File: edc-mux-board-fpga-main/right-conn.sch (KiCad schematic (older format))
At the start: 75 parts, among them J10 Device 7, J6 Power In, J7 Device 4, J8 Device 5, J9 Device 6, Q3 CSD18501Q5A, SW1 Power Switch, U1 LM74610-Q1, U33 R-78B12-2.0

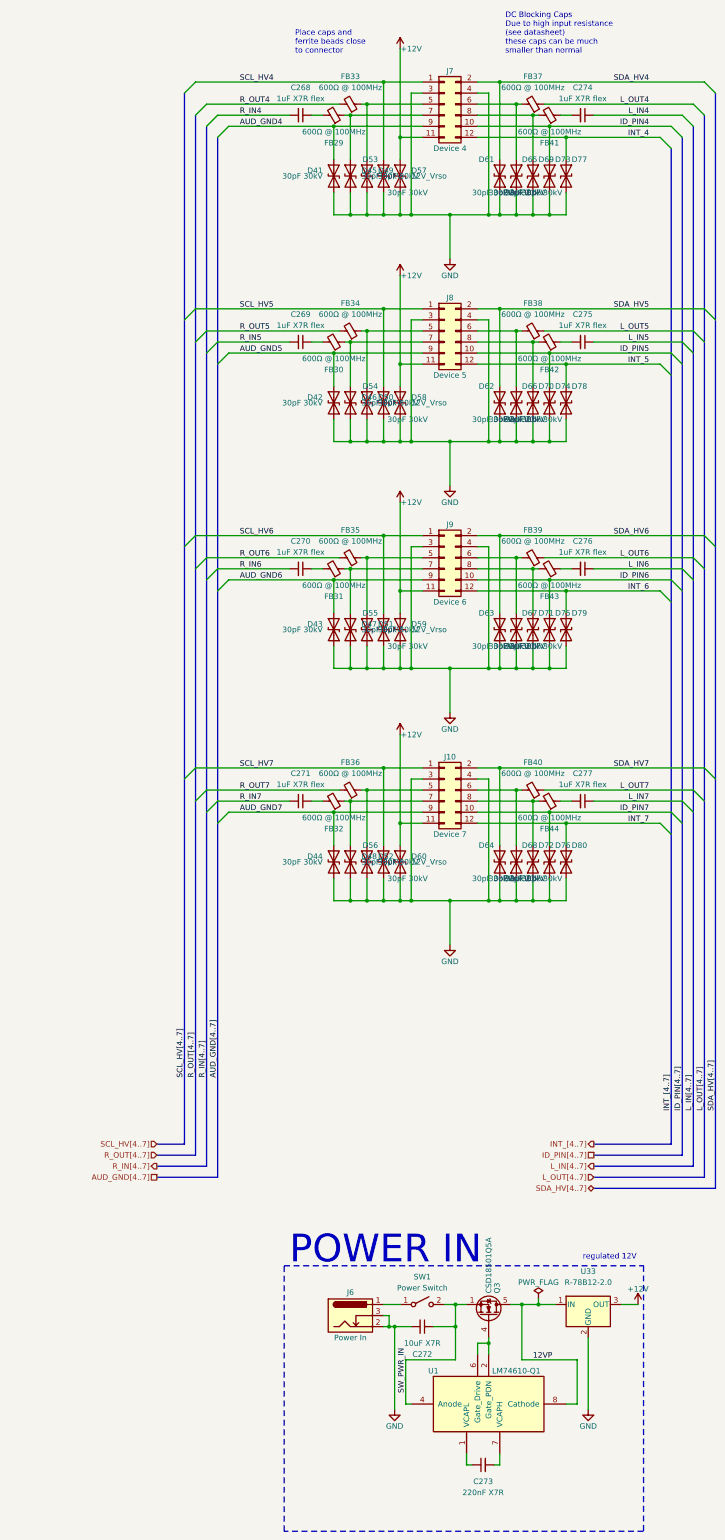
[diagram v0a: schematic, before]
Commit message: migrating right-conn changes from expansion to main
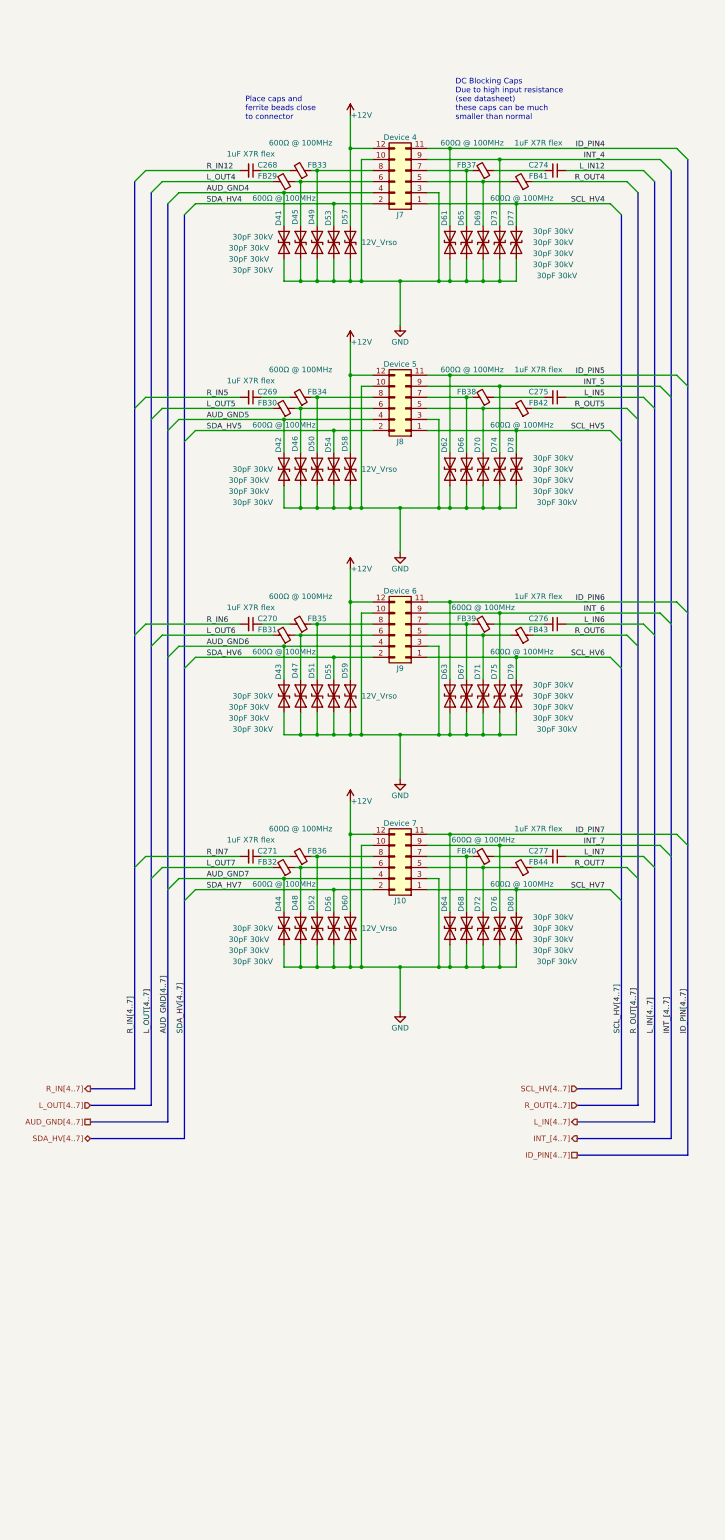
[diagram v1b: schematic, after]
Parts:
- removed C272: 10uF X7R, Capacitor_SMD:C_1206_3216Metric, symbol Device:C_Small
- removed C273: 220nF X7R, Capacitor_SMD:C_0603_1608Metric, symbol Device:C_Small
- removed J6: Power In, SW-Switchcraft:PCL712AS, symbol Connector:Barrel_Jack_Switch
- removed Q3: CSD18501Q5A, Package_TO_SOT_SMD:TDSON-8-1, symbol Transistor_FET:CSD18501Q5A
- removed SW1: Power Switch, Connector_PinHeader_2.54mm:PinHeader_1x02_P2.54mm_Vertical, symbol Switch:SW_SPST
- removed U1: LM74610-Q1, Package_SO:VSSOP-8_3.0x3.0mm_P0.65mm, symbol SW-Texas:LM74610-Q1
- removed U33: R-78B12-2.0, Converter_DCDC:Converter_DCDC_RECOM_R-78B-2.0_THT, symbol Regulator_Switching:R-78B12-2.0
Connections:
- net +12V: now also J10.12 (Pin_12), J7.12 (Pin_12), J8.12 (Pin_12), J9.12 (Pin_12); no longer J10.11 (Pin_11), J7.11 (Pin_11), J8.11 (Pin_11), J9.11 (Pin_11)
- net AUD_GND4: now also J7.4 (Pin_4); no longer J7.9 (Pin_9)
- net AUD_GND5: now also J8.4 (Pin_4); no longer J8.9 (Pin_9)
- net AUD_GND6: now also J9.4 (Pin_4); no longer J9.9 (Pin_9)
- net AUD_GND7: now also J10.4 (Pin_4); no longer J10.9 (Pin_9)
- net GND: now also J10.10 (Pin_10), J7.10 (Pin_10), J8.10 (Pin_10), J9.10 (Pin_10); no longer J10.4 (Pin_4), J7.4 (Pin_4), J8.4 (Pin_4), J9.4 (Pin_4)
- net ID_PIN4: now also D61.1 (A1), J7.11 (Pin_11); no longer D73.1 (A1), J7.10 (Pin_10)
- net ID_PIN5: now also D62.1 (A1), J8.11 (Pin_11); no longer D74.1 (A1), J8.10 (Pin_10)
- net ID_PIN6: now also D63.1 (A1), J9.11 (Pin_11); no longer D75.1 (A1), J9.10 (Pin_10)
- net ID_PIN7: now also D64.1 (A1), J10.11 (Pin_11); no longer D76.1 (A1), J10.10 (Pin_10)
- net INT_4: now also D73.1 (A1), J7.9 (Pin_9); no longer D77.1 (A1), J7.12 (Pin_12)
- net INT_5: now also D74.1 (A1), J8.9 (Pin_9); no longer D78.1 (A1), J8.12 (Pin_12)
- net INT_6: now also D75.1 (A1), J9.9 (Pin_9); no longer D79.1 (A1), J9.12 (Pin_12)
- net INT_7: now also D76.1 (A1), J10.9 (Pin_9); no longer D80.1 (A1), J10.12 (Pin_12)
- net L_OUT4: now also FB29.2; no longer FB37.1
- net L_OUT5: now also FB30.2; no longer FB38.1
- net L_OUT6: now also FB31.2; no longer FB39.1
- net L_OUT7: now also FB32.2; no longer FB40.1
- net R_OUT4: now also FB41.1; no longer FB33.2
- net R_OUT5: now also FB42.1; no longer FB34.2
- net R_OUT6: now also FB43.1; no longer FB35.2
- net R_OUT7: now also FB44.1; no longer FB36.2
- net SCL_HV4: now also D77.1 (A1); no longer D53.1 (A1)
- net SCL_HV5: now also D78.1 (A1); no longer D54.1 (A1)
- net SCL_HV6: now also D79.1 (A1); no longer D55.1 (A1)
- net SCL_HV7: now also D80.1 (A1); no longer D56.1 (A1)
- net SDA_HV4: now also D53.1 (A1); no longer D61.1 (A1)
- net SDA_HV5: now also D54.1 (A1); no longer D62.1 (A1)
- net SDA_HV6: now also D55.1 (A1); no longer D63.1 (A1)
- net SDA_HV7: now also D56.1 (A1); no longer D64.1 (A1)
- net at D49.1 (A1), FB33.1: now also J7.8 (Pin_8); no longer J7.5 (Pin_5)
- net at D65.1 (A1), FB37.2: now also J7.7 (Pin_7); no longer J7.6 (Pin_6)
- net at D45.1 (A1), FB29.1: now also J7.6 (Pin_6); no longer J7.7 (Pin_7)
- net at D69.1 (A1), FB41.2: now also J7.5 (Pin_5); no longer J7.8 (Pin_8)
- net at C268.1: now also FB33.2; no longer FB29.2
- net at C274.2: now also FB37.1; no longer FB41.1
- net at D50.1 (A1), FB34.1: now also J8.8 (Pin_8); no longer J8.5 (Pin_5)
- net at D66.1 (A1), FB38.2: now also J8.7 (Pin_7); no longer J8.6 (Pin_6)
- net at D46.1 (A1), FB30.1: now also J8.6 (Pin_6); no longer J8.7 (Pin_7)
- net at D70.1 (A1), FB42.2: now also J8.5 (Pin_5); no longer J8.8 (Pin_8)
- net at C269.1: now also FB34.2; no longer FB30.2
- net at C275.2: now also FB38.1; no longer FB42.1
- net at D51.1 (A1), FB35.1: now also J9.8 (Pin_8); no longer J9.5 (Pin_5)
- net at D67.1 (A1), FB39.2: now also J9.7 (Pin_7); no longer J9.6 (Pin_6)
- net at D47.1 (A1), FB31.1: now also J9.6 (Pin_6); no longer J9.7 (Pin_7)
- net at D71.1 (A1), FB43.2: now also J9.5 (Pin_5); no longer J9.8 (Pin_8)
- net at C270.1: now also FB35.2; no longer FB31.2
- net at C276.2: now also FB39.1; no longer FB43.1
- net at D52.1 (A1), FB36.1: now also J10.8 (Pin_8); no longer J10.5 (Pin_5)
- net at D68.1 (A1), FB40.2: now also J10.7 (Pin_7); no longer J10.6 (Pin_6)
- net at D48.1 (A1), FB32.1: now also J10.6 (Pin_6); no longer J10.7 (Pin_7)
- net at D72.1 (A1), FB44.2: now also J10.5 (Pin_5); no longer J10.8 (Pin_8)
- net at C271.1: now also FB36.2; no longer FB32.2
- net at C277.2: now also FB40.1; no longer FB44.1
- net L_IN4 renamed L_IN12
- net R_IN4 renamed R_IN12
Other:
- note removed: "POWER IN"
- note removed: "regulated 12V"
- moved on the sheet: C268, C269, C270, C271, C274, C275, C276, C277, D53, D61, FB29, FB30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
